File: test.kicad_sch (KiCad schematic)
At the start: 20 parts, among them J1 Conn_01x04_Pin, J3 XT90PW-F, J4 XT90PW-F, Q1 S8550 2TY DNP SOT-23 SMD 0.5A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, U1 LM741, U3 HX711, U4 MPXV7002DP

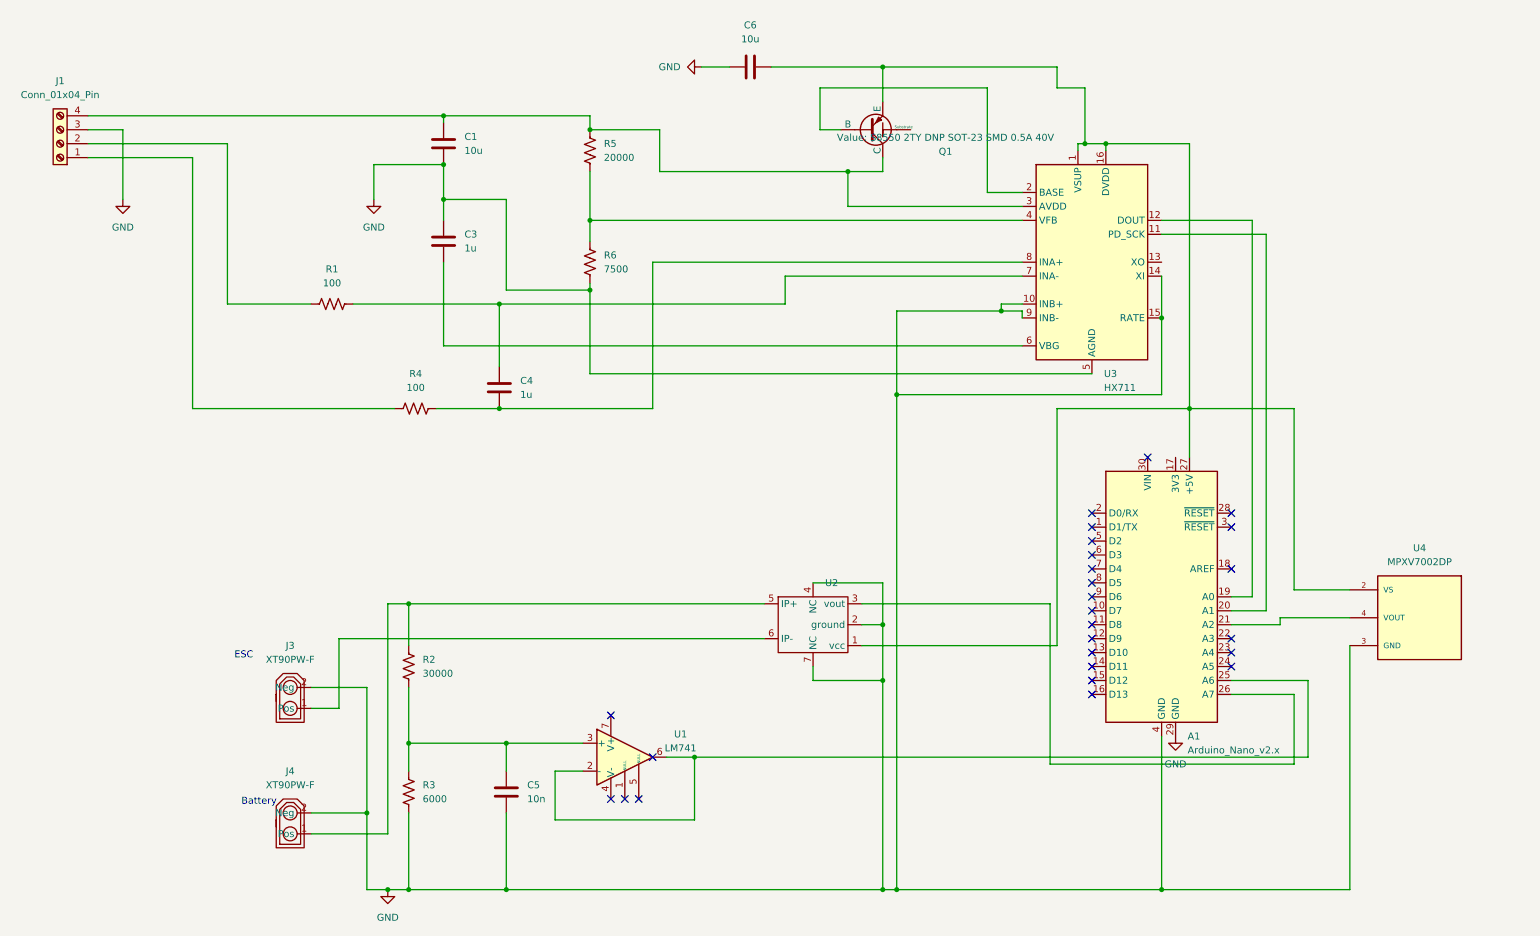
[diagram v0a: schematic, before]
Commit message: Replaced test files
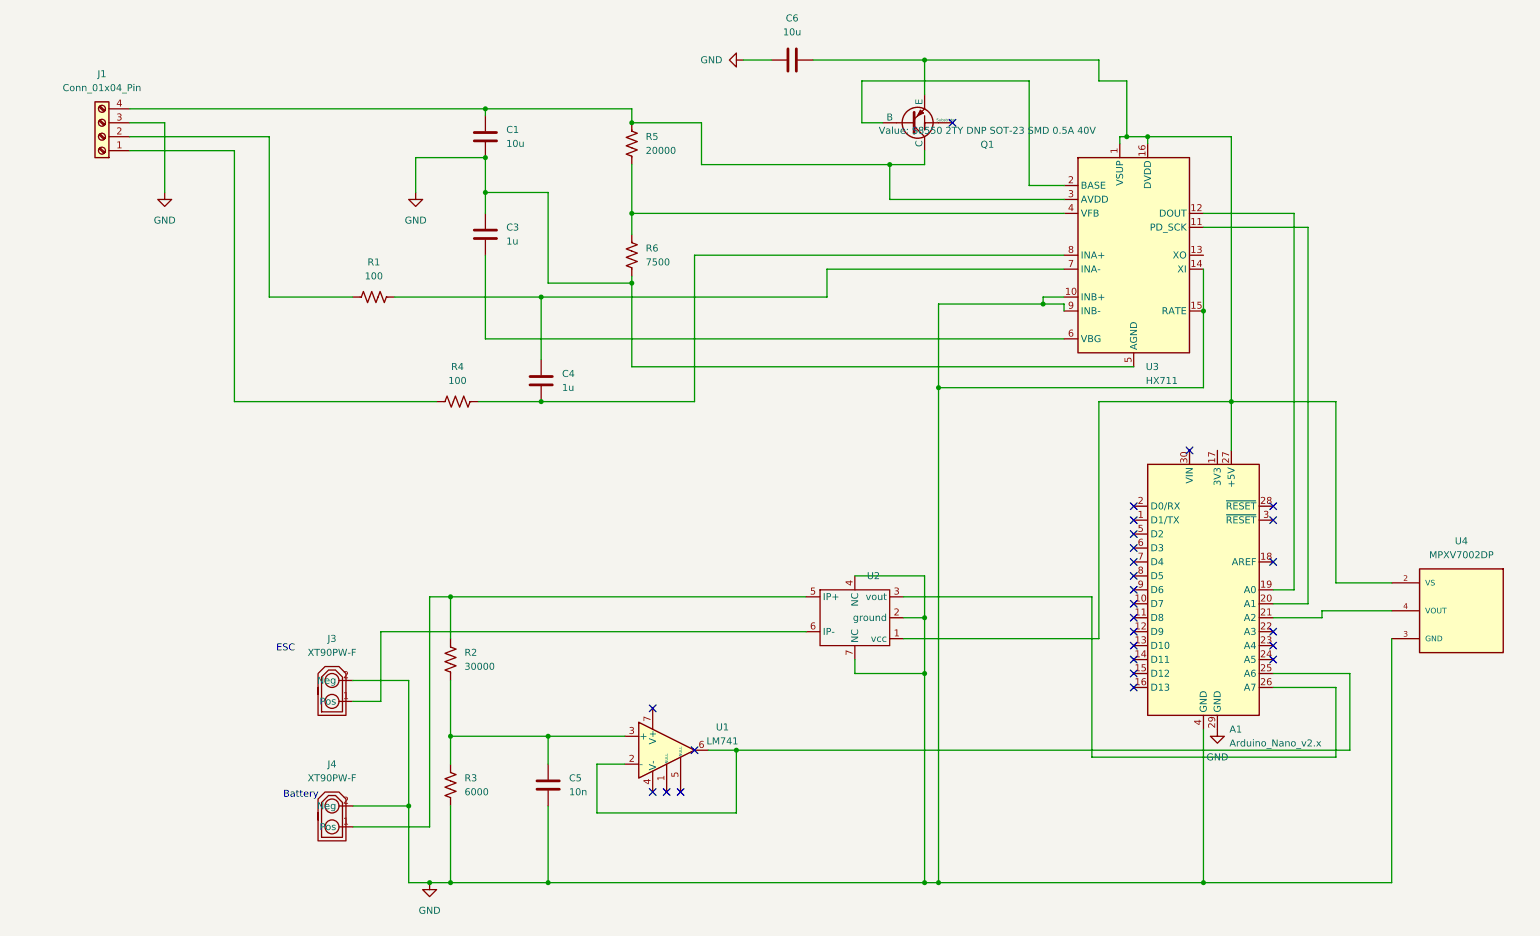
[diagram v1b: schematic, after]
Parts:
- U1: footprint Userlib:LM741 -> digikey-footprints:SOIC-8_W3.9mm
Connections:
- no-connect marks 26 -> 27

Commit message: Raymond fixed nets and added SD card module
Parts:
- added J2: Conn_01x06, Connector_JST:JST_EH_B6B-EH-A_1x06_P2.50mm_Vertical, symbol Connector_Generic:Conn_01x06
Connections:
- net GND: now also J2.6 (Pin_6)
- net at A1.27 (+5V), C6.1, Q1.3 (E)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: now also J2.5 (Pin_5); no longer U2.1 (vcc)
- net at A1.17 (3V3): now also U2.1 (vcc)
- net at A1.5 (D2): now also J2.4 (Pin_4)
- net at A1.6 (D3): now also J2.3 (Pin_3)
- net at A1.7 (D4): now also J2.2 (Pin_2)
- net at A1.8 (D5): now also J2.1 (Pin_1)
- no-connect marks 27 -> 23
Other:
- note added: "Checked"
- note added: "Checked 1x4"
- note added: "Checked C1"
- note added: "Checked C3"
- note added: "Checked C4"
- note added: "Checked C6"
- note added: "Checked R1"
- note added: "Checked R4"
- note added: "Checked R5"
- note added: "Checked R6"
- note added: "Checked Transistor"
- note added: "Checked buffer"
- note added: "Checked magnometer"
- note added: "Micro SD Module"
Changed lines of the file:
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@@
   (junction (at 227.33 173.99) (diameter 0) (color 0 0 0 0)
+  )
+  (junction (at 176.53 118.11) (diameter 0) (color 0 0 0 0)
   )
   (junction (at 232.41 86.36) (diameter 0) (color 0 0 0 0)
@@
   (no_connect (at 134.62 149.86))
   (no_connect (at 214.63 123.19))
-  (no_connect (at 214.63 110.49))
   (no_connect (at 224.79 95.25))
   (no_connect (at 214.63 133.35))
   (no_connect (at 214.63 120.65))
   (no_connect (at 127 142.24))
-  (no_connect (at 214.63 118.11))
   (no_connect (at 214.63 135.89))
   (no_connect (at 240.03 115.57))
@@
   (no_connect (at 181.61 35.56))
   (no_connect (at 129.54 157.48))
-  (no_connect (at 214.63 113.03))
   (no_connect (at 240.03 105.41))
   (no_connect (at 127 157.48))
-  (no_connect (at 214.63 115.57))
   (no_connect (at 214.63 125.73))
   (no_connect (at 240.03 133.35))
+  (wire (pts (xy 205.74 118.11) (xy 214.63 118.11))
+    (stroke (width 0) (type default))
+  )
+  (wire (pts (xy 210.82 100.33) (xy 210.82 110.49))
+    (stroke (width 0) (type default))
+  )
   (wire (pts (xy 212.09 38.1) (xy 213.36 38.1))
     (stroke (width 0) (type default))
@@
     (stroke (width 0) (type default))
   )
+  (wire (pts (xy 229.87 92.71) (xy 193.04 92.71))
+    (stroke (width 0) (type default))
+  )
   (wire (pts (xy 106.68 67.31) (xy 80.01 67.31))
     (stroke (width 0) (type default))
@@
     (stroke (width 0) (type default))
   )
-  (wire (pts (xy 208.28 86.36) (xy 208.28 129.54))
-    (stroke (width 0) (type default))
-  )
   (wire (pts (xy 107.95 160.02) (xy 107.95 173.99))
     (stroke (width 0) (type default))
@@
     (stroke (width 0) (type default))
   )
+  (wire (pts (xy 210.82 110.49) (xy 214.63 110.49))
+    (stroke (width 0) (type default))
+  )
   (wire (pts (xy 254 135.89) (xy 240.03 135.89))
     (stroke (width 0) (type default))
   )
-  (wire (pts (xy 172.72 129.54) (xy 208.28 129.54))
-    (stroke (width 0) (type default))
-  )
   (wire (pts (xy 72.39 160.02) (xy 82.55 160.02))
     (stroke (width 0) (type default))
@@
     (stroke (width 0) (type default))
   )
+  (wire (pts (xy 208.28 113.03) (xy 214.63 113.03))
+    (stroke (width 0) (type default))
+  )
   (wire (pts (xy 107.95 173.99) (xy 90.17 173.99))
     (stroke (width 0) (type default))
@@
     (stroke (width 0) (type default))
   )
+  (wire (pts (xy 205.74 107.95) (xy 205.74 118.11))
+    (stroke (width 0) (type default))
+  )
+  (wire (pts (xy 207.01 105.41) (xy 207.01 115.57))
+    (stroke (width 0) (type default))
+  )
   (wire (pts (xy 72.39 67.31) (xy 57.15 67.31))
     (stroke (width 0) (type default))
@@
     (stroke (width 0) (type default))
   )
+  (wire (pts (xy 193.04 92.71) (xy 193.04 129.54))
+    (stroke (width 0) (type default))
+  )
   (wire (pts (xy 227.33 52.07) (xy 243.84 52.07))
     (stroke (width 0) (type default))
@@
     (stroke (width 0) (type default))
   )
+  (wire (pts (xy 157.48 100.33) (xy 210.82 100.33))
+    (stroke (width 0) (type default))
+  )
   (wire (pts (xy 163.83 135.89) (xy 176.53 135.89))
     (stroke (width 0) (type default))
@@
     (stroke (width 0) (type default))
   )
+  (wire (pts (xy 157.48 95.25) (xy 176.53 95.25))
+    (stroke (width 0) (type default))
+  )
   (wire (pts (xy 261.62 124.46) (xy 248.92 124.46))
     (stroke (width 0) (type default))
@@
     (stroke (width 0) (type default))
   )
+  (wire (pts (xy 157.48 107.95) (xy 205.74 107.95))
+    (stroke (width 0) (type default))
+  )
   (wire (pts (xy 142.24 149.86) (xy 137.16 149.86))
     (stroke (width 0) (type default))
@@
     (stroke (width 0) (type default))
   )
+  (wire (pts (xy 157.48 102.87) (xy 208.28 102.87))
+    (stroke (width 0) (type default))
+  )
   (wire (pts (xy 123.19 64.77) (xy 107.95 64.77))
     (stroke (width 0) (type default))
@@
     (stroke (width 0) (type default))
   )
+  (wire (pts (xy 176.53 95.25) (xy 176.53 118.11))
+    (stroke (width 0) (type default))
+  )
   (wire (pts (xy 135.89 43.18) (xy 135.89 35.56))
     (stroke (width 0) (type default))
@@
     (stroke (width 0) (type default))
   )
+  (wire (pts (xy 157.48 97.79) (xy 210.82 97.79))
+    (stroke (width 0) (type default))
+  )
+  (wire (pts (xy 229.87 95.25) (xy 229.87 92.71))
+    (stroke (width 0) (type default))
+  )
   (wire (pts (xy 172.72 125.73) (xy 176.53 125.73))
     (stroke (width 0) (type default))
@@
     (stroke (width 0) (type default))
   )
+  (wire (pts (xy 193.04 129.54) (xy 172.72 129.54))
+    (stroke (width 0) (type default))
+  )
   (wire (pts (xy 121.92 147.32) (xy 107.95 147.32))
     (stroke (width 0) (type default))
@@
     (stroke (width 0) (type default))
   )
+  (wire (pts (xy 210.82 97.79) (xy 210.82 86.36))
+    (stroke (width 0) (type default))
+  )
   (wire (pts (xy 248.92 125.73) (xy 240.03 125.73))
     (stroke (width 0) (type default))
@@
     (stroke (width 0) (type default))
   )
+  (wire (pts (xy 207.01 115.57) (xy 214.63 115.57))
+    (stroke (width 0) (type default))
+  )
   (wire (pts (xy 198.12 68.58) (xy 179.07 68.58))
     (stroke (width 0) (type default))
@@
     (stroke (width 0) (type default))
   )
+  (wire (pts (xy 210.82 86.36) (xy 232.41 86.36))
+    (stroke (width 0) (type default))
+  )
   (wire (pts (xy 83.82 41.91) (xy 96.52 41.91))
     (stroke (width 0) (type default))
@@
     (stroke (width 0) (type default))
   )
-  (wire (pts (xy 208.28 86.36) (xy 232.41 86.36))
+  (wire (pts (xy 157.48 105.41) (xy 207.01 105.41))
     (stroke (width 0) (type default))
   )
@@
     (stroke (width 0) (type default))
   )
+  (wire (pts (xy 208.28 102.87) (xy 208.28 113.03))
+    (stroke (width 0) (type default))
+  )
+  (text "Checked R4" (at 86.36 91.44 0)
+    (effects (font (size 1.27 1.27)) (justify left bottom))
+  )
+  (text "Checked R6" (at 125.73 57.15 0)
+    (effects (font (size 1.27 1.27)) (justify left bottom))
+  )
+  (text "Checked Transistor" (at 152.4 33.02 0)
+    (effects (font (size 1.27 1.27)) (justify left bottom))
+  )
+  (text "Checked R1" (at 71.12 71.12 0)
+    (effects (font (size 1.27 1.27)) (justify left bottom))
+  )
+  (text "Checked C3" (at 83.82 60.96 0)
+    (effects (font (size 1.27 1.27)) (justify left bottom))
+  )
+  (text "Checked C1" (at 82.55 38.1 0)
+    (effects (font (size 1.27 1.27)) (justify left bottom))
+  )
   (text "Battery" (at 59.69 158.75 0)
     (effects (font (size 1.27 1.27)) (justify left bottom))
   )
   (text "ESC" (at 58.42 132.08 0)
+    (effects (font (size 1.27 1.27)) (justify left bottom))
+  )
+  (text "Checked R5" (at 109.22 40.64 0)
+    (effects (font (size 1.27 1.27)) (justify left bottom))
+  )
+  (text "Micro SD Module" (at 129.54 95.25 0)
+    (effects (font (size 1.27 1.27)) (justify left bottom))
+  )
+  (text "Checked\n" (at 275.59 109.22 0)
+    (effects (font (size 1.27 1.27)) (justify left bottom))
+  )
+  (text "Checked 1x4\n" (at 21.59 24.13 0)
+    (effects (font (size 1.27 1.27)) (justify left bottom))
+  )
+  (text "Checked magnometer" (at 152.4 116.84 0)
+    (effects (font (size 1.27 1.27)) (justify left bottom))
+  )
+  (text "Checked C4" (at 114.3 83.82 0)
+    (effects (font (size 1.27 1.27)) (justify left bottom))
+  )
+  (text "Checked buffer" (at 129.54 140.97 0)
+    (effects (font (size 1.27 1.27)) (justify left bottom))
+  )
+  (text "Checked C6" (at 154.94 22.86 0)
     (effects (font (size 1.27 1.27)) (justify left bottom))
   )
@@
         )
       )
+    )
+  )
+  (symbol (lib_id "Connector_Generic:Conn_01x06") (at 152.4 102.87 180) (unit 1)
+    (in_bom yes) (on_board yes) (dnp no) (fields_autoplaced)
+    (property "Reference" "J2" (at 152.4 88.9 0)
+      (effects (font (size 1.27 1.27)))
+    )
+    (property "Value" "Conn_01x06" (at 152.4 91.44 0)
+      (effects (font (size 1.27 1.27)))
+    )
+    (property "Footprint" "Connector_JST:JST_EH_B6B-EH-A_1x06_P2.50mm_Vertical" (at 152.4 102.87 0)
+      (effects (font (size 1.27 1.27)) hide)
+    )
+    (property "Datasheet" "~" (at 152.4 102.87 0)
+      (effects (font (size 1.27 1.27)) hide)
+    )
+    (pin "1")
+    (pin "2")
+    (pin "3")
+    (pin "4")
+    (pin "5")
+    (pin "6")
+    (instances
+      (project "Test"
+        (path "/5de3e6fd-b8e3-4ef4-89d0-61c729b79836"
+          (reference "J2") (unit 1)
+        )
+      )

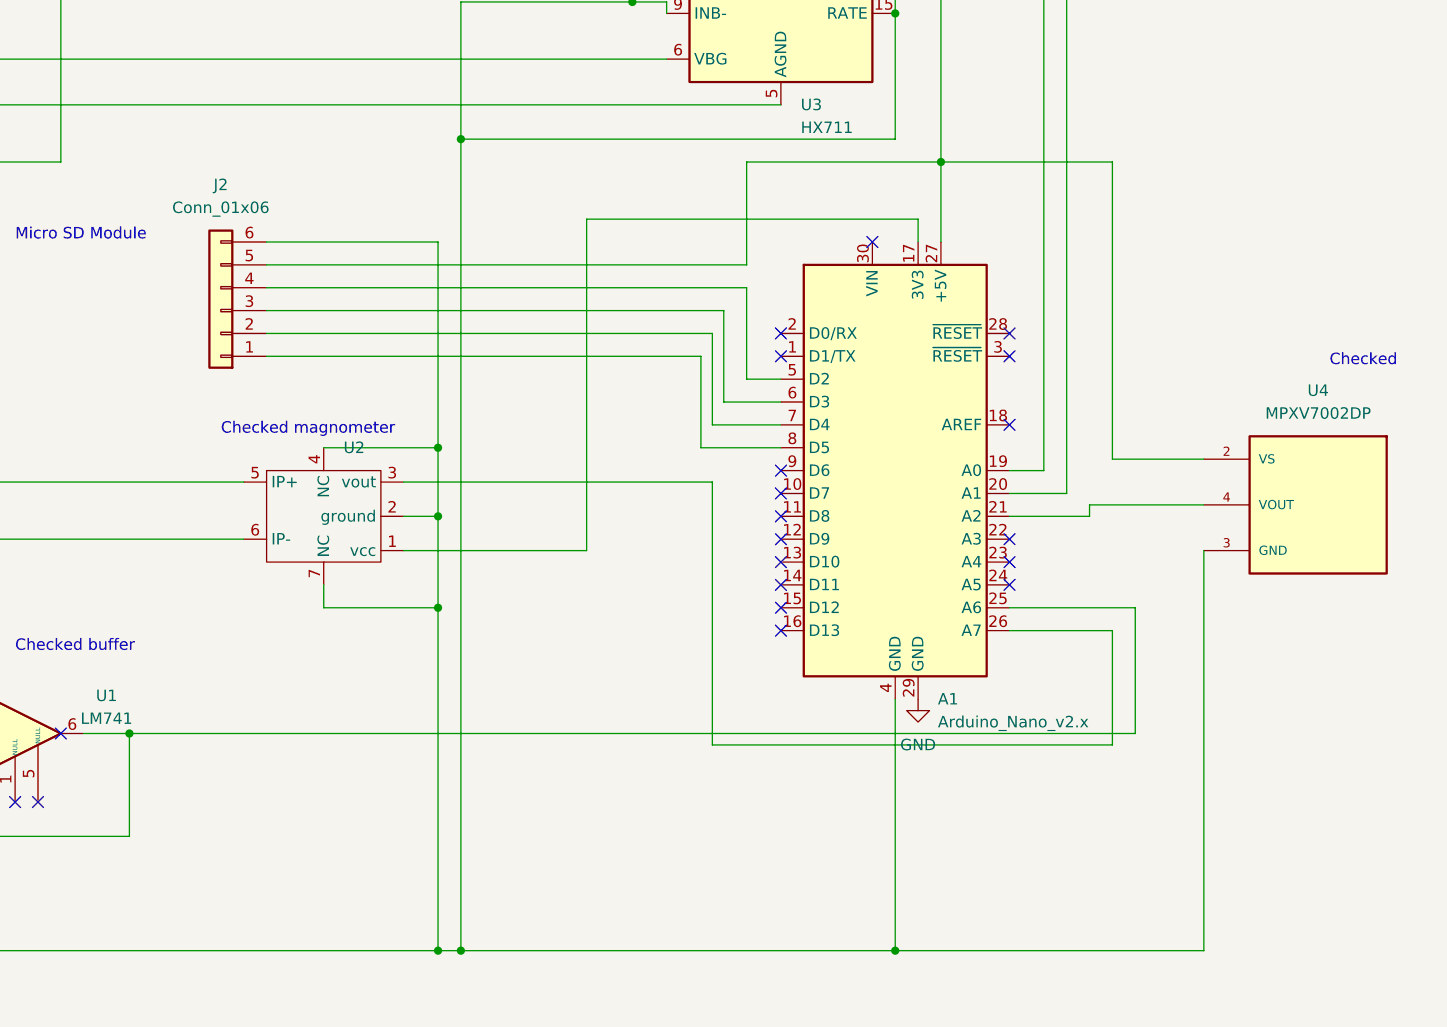
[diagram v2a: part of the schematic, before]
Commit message: Fixed the SD Card
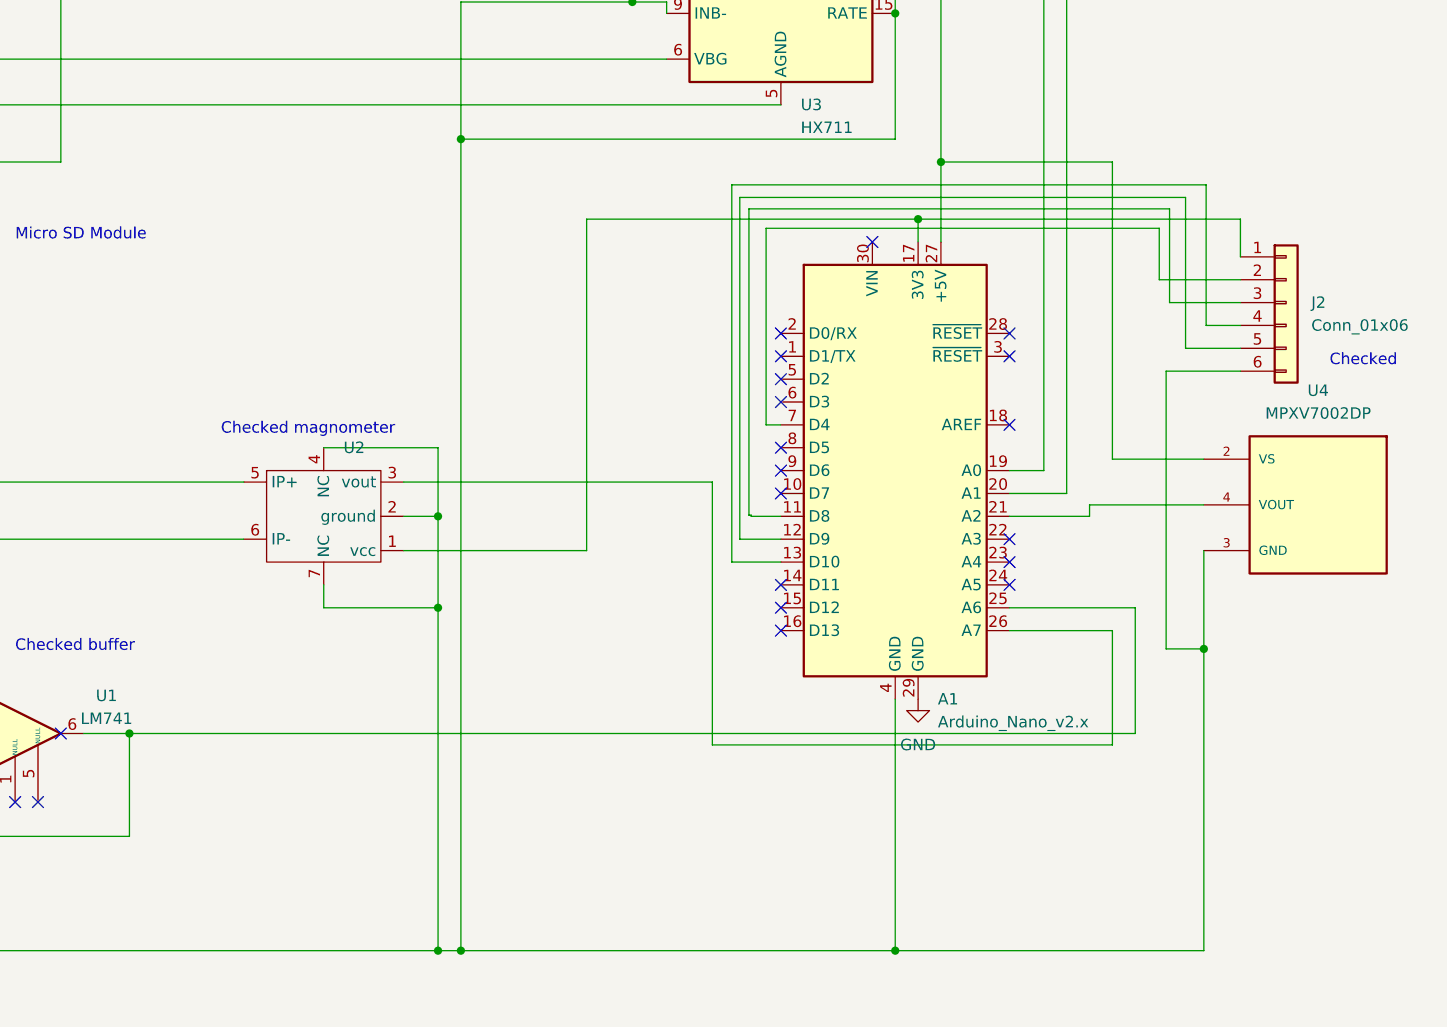
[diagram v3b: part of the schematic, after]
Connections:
- net at A1.27 (+5V), C6.1, Q1.3 (E)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: no longer J2.5 (Pin_5)
- net at A1.11 (D8): now also J2.3 (Pin_3)
- net at A1.12 (D9): now also J2.5 (Pin_5)
- net at A1.13 (D10): now also J2.4 (Pin_4)
- net at A1.17 (3V3), U2.1 (vcc): now also J2.1 (Pin_1)
- net at A1.5 (D2): no longer J2.4 (Pin_4)
- net at A1.6 (D3): no longer J2.3 (Pin_3)
- net at A1.8 (D5): no longer J2.1 (Pin_1)
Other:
- moved on the sheet: J2

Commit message: Fixed caps and generated the gerber and drill files
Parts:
- C3, C4: value 1u -> .1u
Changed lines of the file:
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@@
       (effects (font (size 1.27 1.27)) (justify left))
     )
-    (property "Value" "1u" (at 110.49 83.82 0)
+    (property "Value" ".1u" (at 110.49 83.82 0)
       (effects (font (size 1.27 1.27)) (justify left))
     )
@@
       (effects (font (size 1.27 1.27)) (justify left))
     )
-    (property "Value" "1u" (at 100.33 57.15 0)
-      (effects (font (size 1.27 1.27)) (justify left))
-    )
+    (property "Value" ".1u" (at 100.33 57.15 0)
+      (effects (font (size 1.27 1.27)) (justify left))
+    )
